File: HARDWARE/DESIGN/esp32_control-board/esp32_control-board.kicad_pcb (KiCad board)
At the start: 2 copper layers, 120 x 85 mm, 144 parts, among them J101 Power-in, J201 RFID-module1, J204 USB-prog, J4 Termination, J401 CAN, J402 I2C, J403 UART, J405 Din1, J406 Din3, J407 Din2, J408 Din4, J409 Lock1, J410 Lock2, J411 Ain2, J412 Ain1, J413 Leds, Q102 DMP3013SFV-7, Q401 AO3401A, Q402 BSS138, Q403 BSS138, Q404 AO3401A, SW201 Boot, SW202 Reset, U101 LM63615DQDRRRQ1, U102 AMS1117-3.3, U203 ESP32-S3-WROOM-1U, U204 USBLC6-2SC6, U205 USBLC6-2SC6, U401 SN74LVC125ADR, U409 PC817, U410 PC817, U411 PC817, U412 PC817, U6 TCAN330

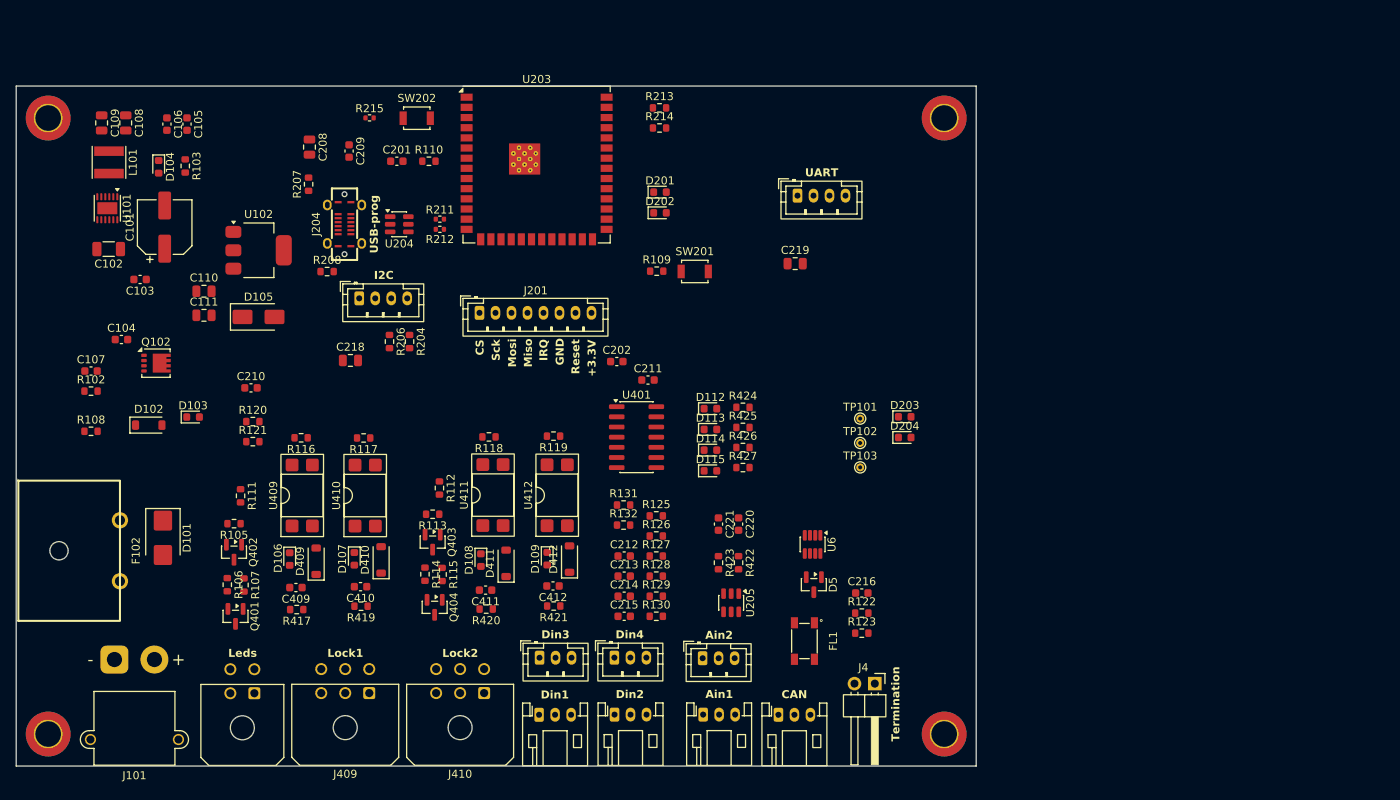
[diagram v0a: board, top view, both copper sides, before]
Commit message: 60908 - PCB-layout updated
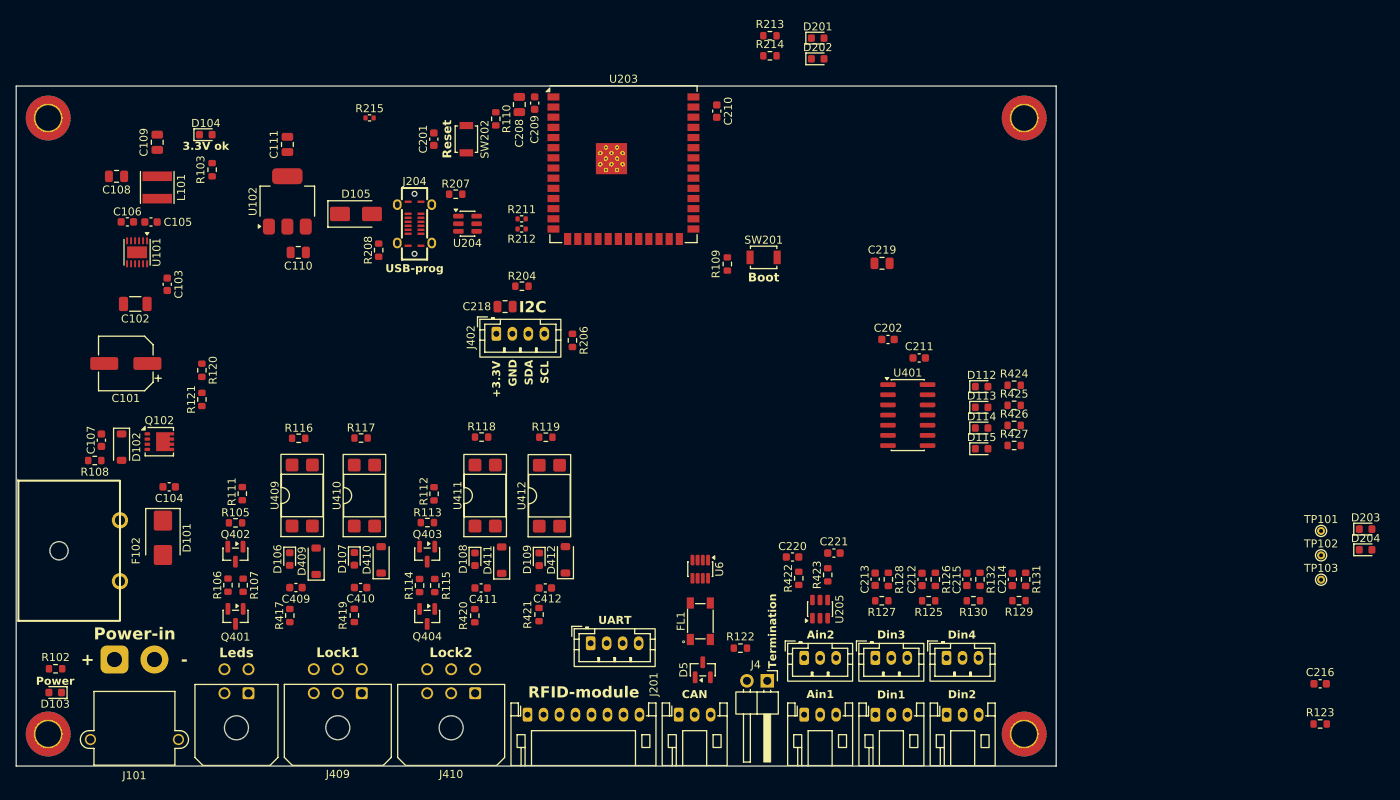
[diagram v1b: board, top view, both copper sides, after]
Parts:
- D103: value 12V ok -> Power
- D104: value +3.3V ok -> 3.3V ok
- J201: value RFID-module1 -> RFID-module; footprint Connector_JST:JST_PH_B8B-PH-K_1x08_P2.00mm_Vertical -> Connector_JST:JST_PH_S8B-PH-K_1x08_P2.00mm_Horizontal
- moved C210 67.7 mm to (157.8, 73.0), turned to -90 degrees
- moved J403 61.6 mm to (142.1, 139.6)
- moved D203 59.3 mm to (238.9, 125.3)
- moved D204 59.3 mm to (238.9, 127.9)
- moved TP101 59.3 mm to (233.4, 125.5)
- moved TP102 59.3 mm to (233.4, 128.6)
- moved TP103 59.3 mm to (233.4, 131.6)
- moved C216 58.4 mm to (233.2, 144.6)
- moved R123 58.4 mm to (233.2, 149.7)
- moved R131 51.1 mm to (196.4, 131.6), turned to 90 degrees
- moved J201 50.6 mm to (134.2, 148.5)
- moved C214 48.6 mm to (194.8, 131.6), turned to -90 degrees
- moved R129 45.3 mm to (195.6, 134.2), turned to 180 degrees
- moved R132 45.1 mm to (190.7, 131.6), turned to 90 degrees
- moved C215 43.1 mm to (189.1, 131.6), turned to -90 degrees
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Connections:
- J401 pad 1: CAN+_conn. -> GND
- J401 pad 3: GND -> CAN+_conn.
- U203 pad 38: unconnected-(U203-IO2-Pad38) -> ai_BatteryVoltage
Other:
- board size 120 x 85 mm -> 130 x 85 mm
- board text added: "+"
- board text added: "-"
- board text added: "CAN+"
- board text added: "CAN-"
- board text added: "SCL"
- board text added: "SDA"

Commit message: 60911 - PCB-layout updated
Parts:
- removed C109: 22u, Capacitor_SMD:C_0805_2012Metric
- removed D201: MCU ok, LED_SMD:LED_0603_1608Metric
- added R216: 1k, Resistor_SMD:R_0603_1608Metric, F.Cu at (147.1, 97.8)
- moved TP101 153.3 mm to (84.6, 88.7), turned to 90 degrees
- moved TP102 151.1 mm to (87.6, 88.7), turned to 90 degrees
- moved TP103 149.0 mm to (90.7, 88.7), turned to 90 degrees
- moved R123 83.7 mm to (151.7, 130.6), turned to -90 degrees
- moved C216 79.7 mm to (155.8, 126.1), turned to -90 degrees
- moved D203 65.6 mm to (181.4, 93.7)
- moved D204 65.6 mm to (181.4, 96.3)
- moved C202 51.9 mm to (149.0, 143.8)
- moved C219 51.4 mm to (144.0, 130.2), turned to 180 degrees
- moved R213 37.8 mm to (187.2, 93.8)
- moved R214 37.8 mm to (187.2, 96.3)
- moved D104 31.5 mm to (105.6, 105.2)
- moved C108 30.8 mm to (110.2, 95.3), turned to 90 degrees
- moved D202 29.9 mm to (187.2, 91.3)
- moved R103 28.6 mm to (110.2, 104.4), turned to -90 degrees
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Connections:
- D202 pad 1: GND_MCU -> unconnected-(D202-K-Pad1)
- D202 pad 2: Net-(D202-A) -> unconnected-(D202-A-Pad2)
- D203 pad 1: unconnected-(D203-K-Pad1) -> GND_MCU
- D203 pad 2: unconnected-(D203-A-Pad2) -> Net-(D203-A)
- D204 pad 1: unconnected-(D204-K-Pad1) -> GND_MCU
- D204 pad 2: unconnected-(D204-A-Pad2) -> Net-(D204-A)
- R213 pad 1: esp_LED_green -> esp_LED_blue
- R213 pad 2: Net-(D201-A) -> Net-(D203-A)
- R214 pad 2: Net-(D202-A) -> Net-(D204-A)
- U203 pad 10: unconnected-(U203-IO17-Pad10) -> Net-(U203-IO17)
- U203 pad 11: unconnected-(U203-IO18-Pad11) -> ctrl_LOCK2_3V3
- U203 pad 22: unconnected-(U203-IO14-Pad22) -> RFID1_irq
- U203 pad 23: unconnected-(U203-IO21-Pad23) -> sens_LOCK1_latch_3V3
- U203 pad 24: unconnected-(U203-IO47-Pad24) -> esp_TCAN330_ctrl-Silent
- U203 pad 25: unconnected-(U203-IO48-Pad25) -> esp_TCAN330_ctrl-Shutdown
- U203 pad 31: unconnected-(U203-IO38-Pad31) -> sens_LOCK2_latch_3V3
- U203 pad 32: unconnected-(U203-IO39-Pad32) -> sens_LOCK2_door_3V3
- U203 pad 33: unconnected-(U203-IO40-Pad33) -> sens_LOCK1_door_3V3
- U203 pad 34: unconnected-(U203-IO41-Pad34) -> esp_LED_red
- U203 pad 35: unconnected-(U203-IO42-Pad35) -> esp_LED_blue
- U203 pad 9: RFID1_irq -> ctrl_LOCK1_3V3
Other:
- board size 130 x 85 mm -> 130 x 70 mm
- board text added: "A-in1"
- board text added: "D-in1"
- board text added: "D-in2"
- board text added: "D-in4"
- board text added: "RxD"
- board text added: "TxD"
